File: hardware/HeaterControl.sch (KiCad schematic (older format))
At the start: 17 parts, among them J1 UART, J2 BTN, J3 OLED, P1 TC2030-CTX, Q1 NX7002AK.215, Q2 NX7002AK.215, SW1 RESET, U1 DS18B20, U2 BL654, U3 SHT30-DIS-B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

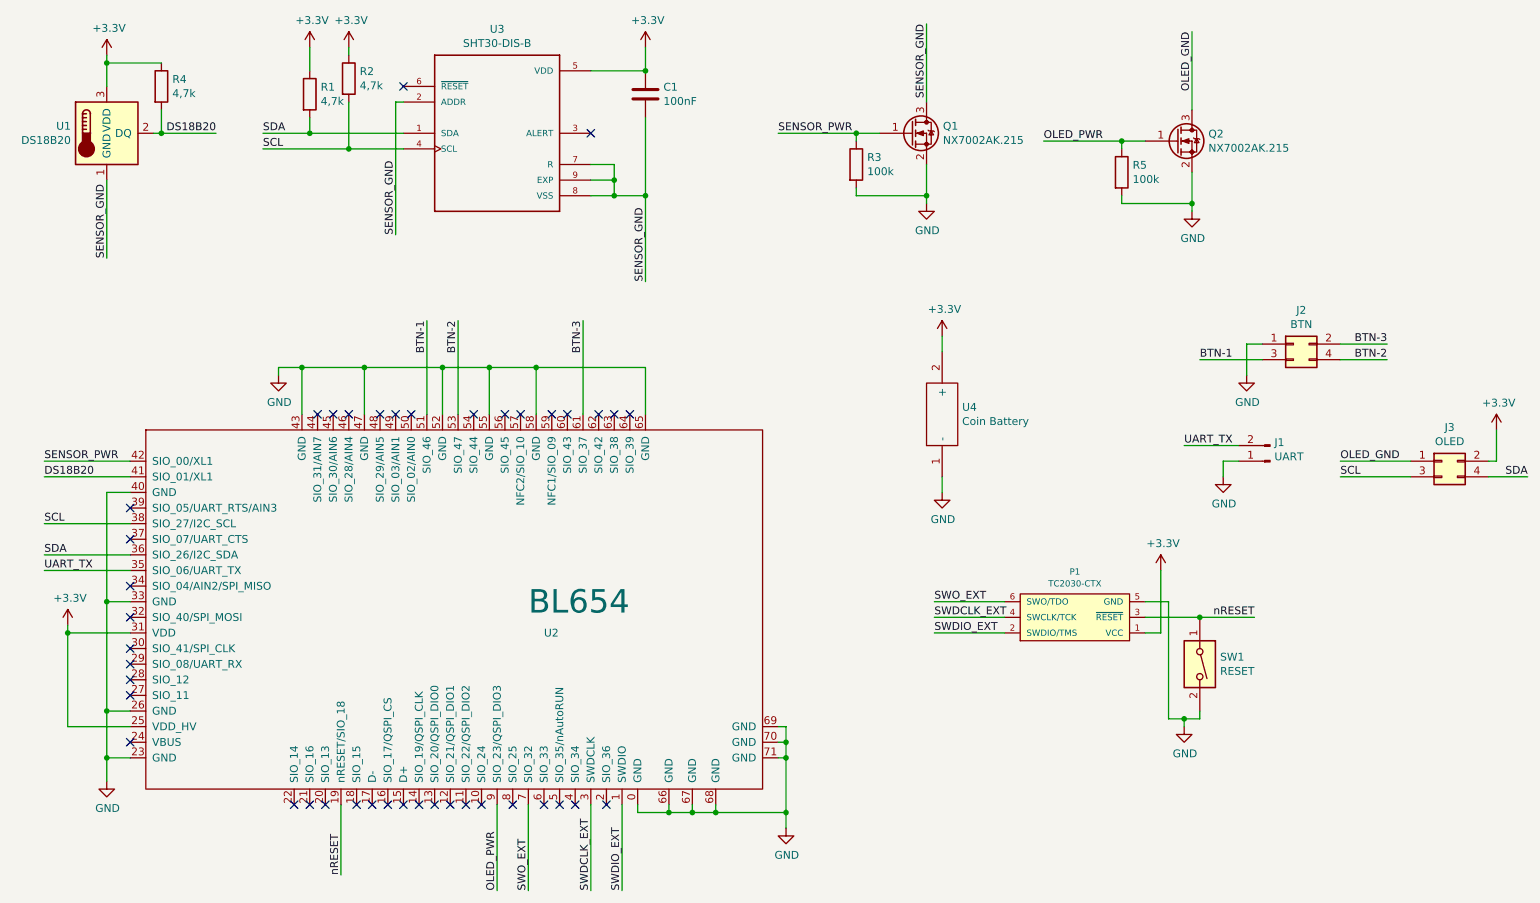
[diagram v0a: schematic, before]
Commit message: Removed Sensor/Oled PWR circuts
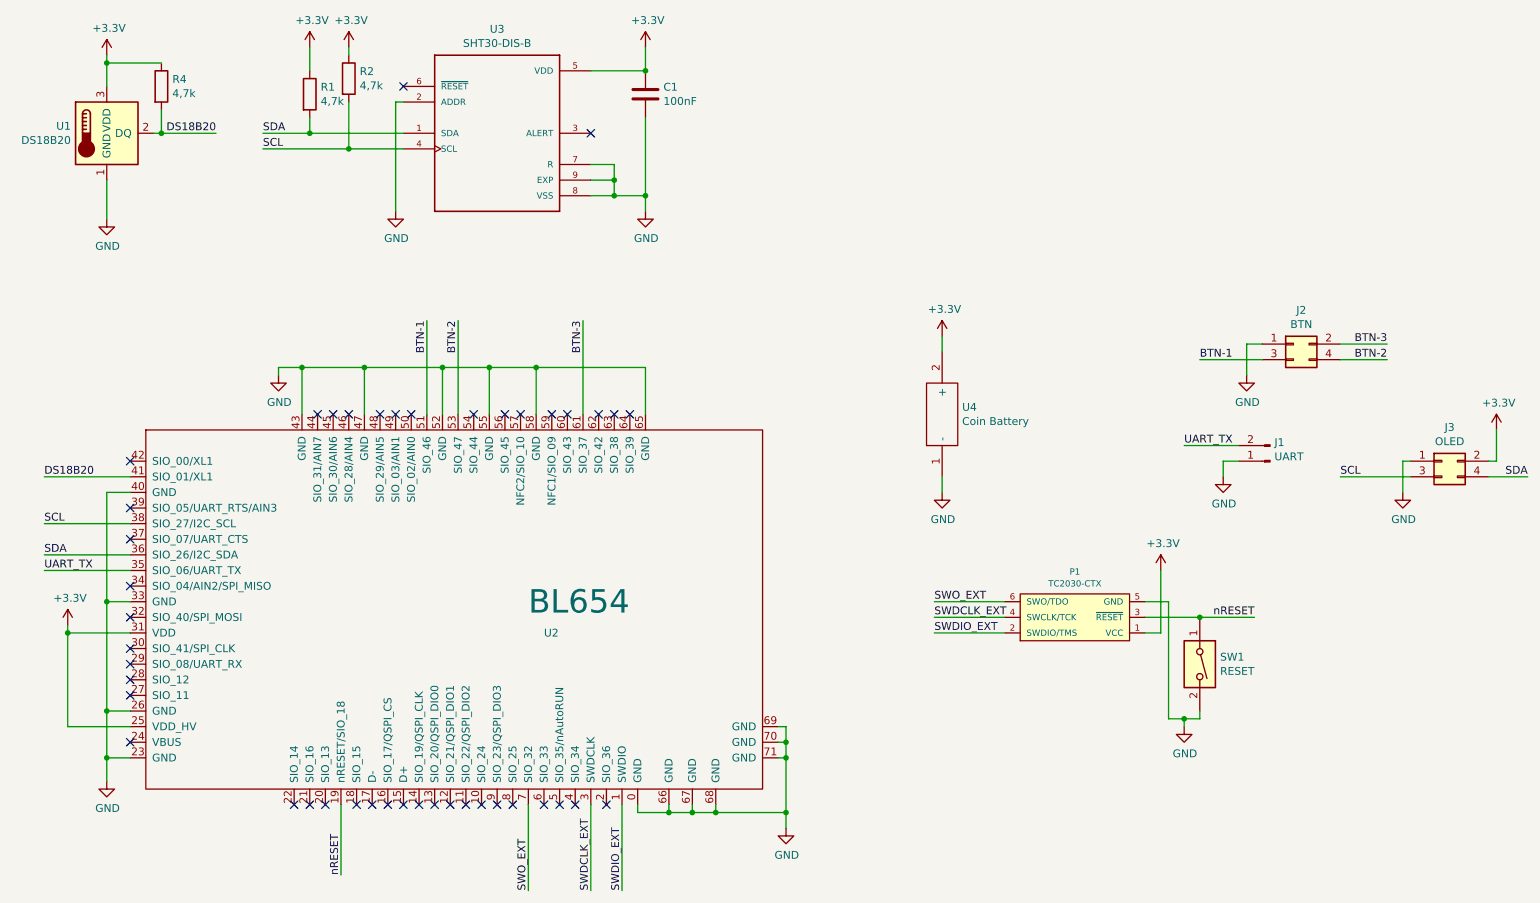
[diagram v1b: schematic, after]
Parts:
- removed Q1, Q2: NX7002AK.215, Package_TO_SOT_SMD:SOT-23, symbol Device:Q_NMOS_GSD
- removed R3, R5: 100k, Resistor_SMD:R_1206_3216Metric, symbol Device:R
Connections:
- net OLED_GND is gone; now on net GND: J3.1 (Pin_1)
- net SENSOR_GND is gone; now on net GND: C1.2, U1.1 (GND), U3.2 (ADDR), U3.7 (R), U3.8 (VSS), U3.9 (EXP)
- net OLED_PWR: no longer names the net of U2.9 (SIO_23/QSPI_DIO3)
- net SENSOR_PWR: no longer names the net of U2.42 (SIO_00/XL1)
- no-connect marks 42 -> 44
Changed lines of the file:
@@
 NoConn ~ 3700 1550
-$Comp
-L Device:Q_NMOS_GSD Q1
-U 1 1 5C695AC0
-P 6950 1850
-F 0 "Q1" H 7155 1896 50  0000 L CNN
-F 1 "NX7002AK.215" H 7155 1805 50  0000 L CNN
-F 2 "Package_TO_SOT_SMD:SOT-23" H 7150 1950 50  0001 C CNN
-F 3 "~" H 6950 1850 50  0001 C CNN
-	1    6950 1850
-	1    0    0    -1
-$EndComp
-$Comp
-L power:GND #PWR0115
-U 1 1 5C695B67
-P 7050 2300
-F 0 "#PWR0115" H 7050 2050 50  0001 C CNN
-F 1 "GND" H 7055 2127 50  0000 C CNN
-F 2 "" H 7050 2300 50  0001 C CNN
-F 3 "" H 7050 2300 50  0001 C CNN
-	1    7050 2300
-	1    0    0    -1
-$EndComp
-Wire Wire Line
-	7050 2300 7050 2250
-$Comp
-L Device:R R3
-U 1 1 5C6978A7
-P 6600 2050
-F 0 "R3" H 6670 2096 50  0000 L CNN
-F 1 "100k" H 6670 2005 50  0000 L CNN
-F 2 "Resistor_SMD:R_1206_3216Metric" V 6530 2050 50  0001 C CNN
-F 3 "~" H 6600 2050 50  0001 C CNN
-	1    6600 2050
-	1    0    0    -1
-$EndComp
-Wire Wire Line
-	6600 1850 6600 1900
-Connection ~ 6600 1850
-Wire Wire Line
-	6600 1850 6750 1850
-Wire Wire Line
-	6600 2200 6600 2250
-Text Label 6100 1850 0    50   ~ 0
-SENSOR_PWR
-Wire Wire Line
-	6100 1850 6600 1850
-Text Label 7050 1150 3    50   ~ 0
-SENSOR_GND
-Wire Wire Line
-	7050 1150 7050 1650
-Wire Wire Line
-	6600 2250 7050 2250
-Connection ~ 7050 2250
-Wire Wire Line
-	7050 2250 7050 2050
 $Comp
 L Sensor_Temperature:DS18B20 U1
@@
 	1    0    0    -1
 $EndComp
-Text Label 1800 2650 1    50   ~ 0
-SENSOR_GND
-Wire Wire Line
-	1800 2150 1800 2650
 Wire Wire Line
 	1800 1550 1800 1400
@@
 	1    0    0    -1
 $EndComp
-Text Label 1400 3950 0    50   ~ 0
-SENSOR_PWR
 Text Label 1400 4050 0    50   ~ 0
 DS18B20
@@
 	4900 2250 5050 2250
 Wire Wire Line
-	5250 2250 5250 2800
-Text Label 5250 2800 1    50   ~ 0
-SENSOR_GND
-Text Label 3650 2500 1    50   ~ 0
-SENSOR_GND
-Wire Wire Line
-	3650 1650 3650 2500
+	3650 1650 3650 2350
 Wire Wire Line
 	4900 1450 5250 1450
 Wire Wire Line
 	5250 1750 5250 2250
-Connection ~ 5250 2250
 $Comp
 L BS-3:BS-3 U4
@@
 Wire Wire Line
 	1950 4050 1400 4050
-Wire Wire Line
-	1950 3950 1400 3950
 NoConn ~ 1950 5350
 $Comp
@@
 Text Label 10000 3200 2    50   ~ 0
 BTN-3
-$Comp
-L Device:Q_NMOS_GSD Q2
-U 1 1 5CA17FC7
-P 8650 1900
-F 0 "Q2" H 8855 1946 50  0000 L CNN
-F 1 "NX7002AK.215" H 8855 1855 50  0000 L CNN
-F 2 "Package_TO_SOT_SMD:SOT-23" H 8850 2000 50  0001 C CNN
-F 3 "~" H 8650 1900 50  0001 C CNN
-	1    8650 1900
-	1    0    0    -1
-$EndComp
-$Comp
-L power:GND #PWR0114
-U 1 1 5CA17FCE
-P 8750 2350
-F 0 "#PWR0114" H 8750 2100 50  0001 C CNN
-F 1 "GND" H 8755 2177 50  0000 C CNN
-F 2 "" H 8750 2350 50  0001 C CNN
-F 3 "" H 8750 2350 50  0001 C CNN
-	1    8750 2350
-	1    0    0    -1
-$EndComp
-Wire Wire Line
-	8750 2350 8750 2300
-$Comp
-L Device:R R5
-U 1 1 5CA17FD5
-P 8300 2100
-F 0 "R5" H 8370 2146 50  0000 L CNN
-F 1 "100k" H 8370 2055 50  0000 L CNN
-F 2 "Resistor_SMD:R_1206_3216Metric" V 8230 2100 50  0001 C CNN
-F 3 "~" H 8300 2100 50  0001 C CNN
-	1    8300 2100
-	1    0    0    -1
-$EndComp
-Wire Wire Line
-	8300 1900 8300 1950
-Connection ~ 8300 1900
-Wire Wire Line
-	8300 1900 8450 1900
-Wire Wire Line
-	8300 2250 8300 2300
-Text Label 7800 1900 0    50   ~ 0
-OLED_PWR
-Wire Wire Line
-	7800 1900 8300 1900
-Text Label 8750 1200 3    50   ~ 0
-OLED_GND
-Wire Wire Line
-	8750 1200 8750 1700
-Wire Wire Line
-	8300 2300 8750 2300
-Connection ~ 8750 2300
-Wire Wire Line
-	8750 2300 8750 2100
-Text Label 9700 3950 0    50   ~ 0
-OLED_GND
 Wire Wire Line
 	4850 3650 4850 3050
@@
 Text Label 4850 3050 3    50   ~ 0
 BTN-3
-Text Label 4300 6700 1    50   ~ 0
-OLED_PWR
-Wire Wire Line
-	4300 6150 4300 6700
 $Comp
 L Connector_Generic:Conn_02x02_Odd_Even J2
@@
 $EndComp
 Wire Wire Line
-	9700 3950 10150 3950
-Wire Wire Line
 	10900 4050 10650 4050
 Wire Wire Line
@@
 Wire Wire Line
 	9700 4050 10150 4050
+$Comp
+L power:GND #PWR?
+U 1 1 5CB2C1A7
+P 5250 2350
+F 0 "#PWR?" H 5250 2100 50  0001 C CNN
+F 1 "GND" H 5255 2177 50  0000 C CNN
+F 2 "" H 5250 2350 50  0001 C CNN
+F 3 "" H 5250 2350 50  0001 C CNN
+	1    5250 2350
+	1    0    0    -1
+$EndComp
+Wire Wire Line
+	5250 2250 5250 2350
+Connection ~ 5250 2250
+$Comp
+L power:GND #PWR?
+U 1 1 5CB36B32
+P 3650 2350
+F 0 "#PWR?" H 3650 2100 50  0001 C CNN
+F 1 "GND" H 3655 2177 50  0000 C CNN
+F 2 "" H 3650 2350 50  0001 C CNN
+F 3 "" H 3650 2350 50  0001 C CNN
+	1    3650 2350
+	1    0    0    -1
+$EndComp
+$Comp
+L power:GND #PWR?
+U 1 1 5CB396B8
+P 1800 2400
+F 0 "#PWR?" H 1800 2150 50  0001 C CNN
+F 1 "GND" H 1805 2227 50  0000 C CNN
+F 2 "" H 1800 2400 50  0001 C CNN
+F 3 "" H 1800 2400 50  0001 C CNN
+	1    1800 2400
+	1    0    0    -1
+$EndComp
+Wire Wire Line
+	1800 2400 1800 2150
+$Comp
+L power:GND #PWR?
+U 1 1 5CB51F1E
+P 10100 4150
+F 0 "#PWR?" H 10100 3900 50  0001 C CNN
+F 1 "GND" H 10105 3977 50  0000 C CNN
+F 2 "" H 10100 4150 50  0001 C CNN
+F 3 "" H 10100 4150 50  0001 C CNN
+	1    10100 4150
+	1    0    0    -1
+$EndComp
+Wire Wire Line
+	10100 4150 10100 3950
+Wire Wire Line
+	10100 3950 10150 3950
+NoConn ~ 1950 3950
+NoConn ~ 4300 6150
 $EndSCHEMATC
